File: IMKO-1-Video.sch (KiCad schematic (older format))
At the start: 20 parts, among them U18 82S129, U19 74LS244, U20 74LS244, U22 74LS32, U23 74LS86, U24 74LS163, U25 74LS00, U26 74LS374

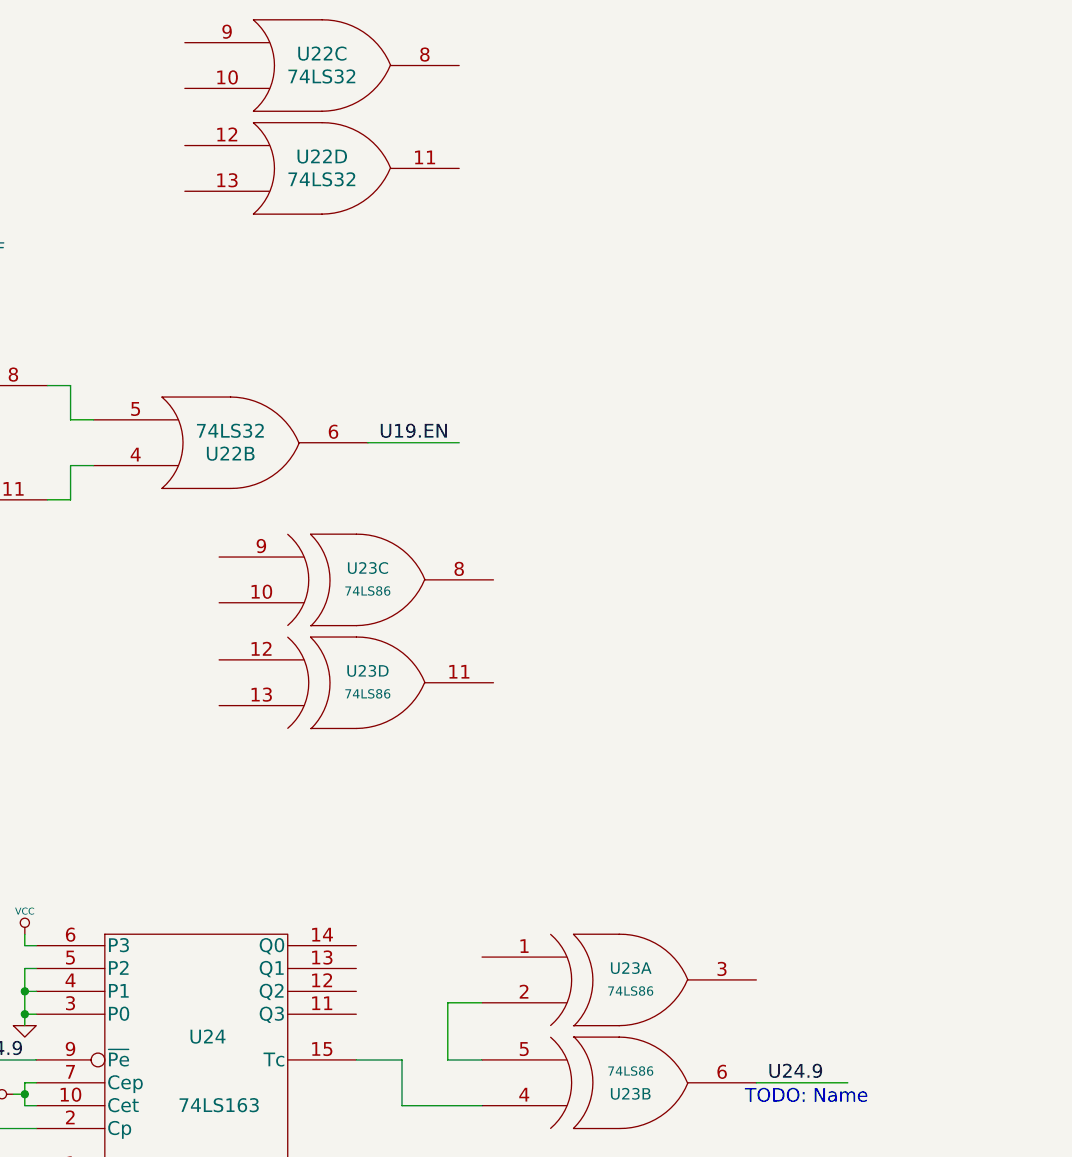
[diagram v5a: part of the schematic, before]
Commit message: Added SFF96364
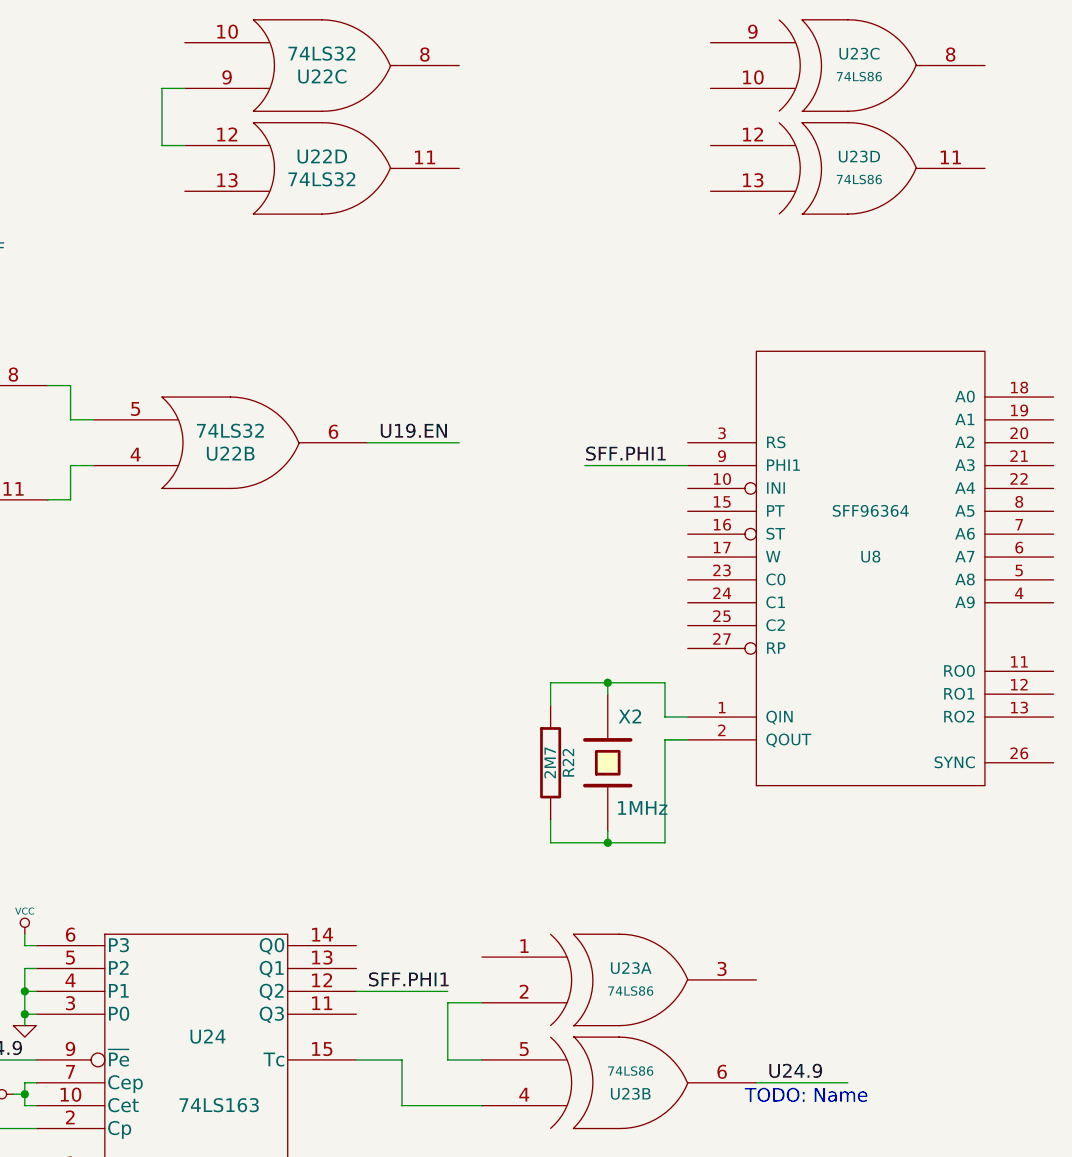
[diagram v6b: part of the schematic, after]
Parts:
- added R22: 2M7, symbol R
- added U8: SFF96364, MODULE, symbol SFF96364
- added X2: 1MHz, symbol CRYSTAL
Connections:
- net labels added: SFF.PHI1
- wire segments 148 -> 163
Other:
- moved on the sheet: U23C, U23D
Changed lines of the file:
@@
-EESchema Schematic File Version 2  date Wed 10 Oct 2012 11:46:42 PM EEST
+EESchema Schematic File Version 2  date Thu 11 Oct 2012 11:02:29 PM EEST
 LIBS:power
 LIBS:device
@@
 LIBS:valves
 LIBS:o_memory
+LIBS:SFF96364
 LIBS:IMKO-1-Video-cache
 EELAYER 27 0
@@
 Sheet 1 1
 Title "noname.sch"
-Date "10 oct 2012"
+Date "11 oct 2012"
 Rev ""
 Comp ""
@@
 L 74LS86 U23
 U 3 1 5075BC19
-P 9750 5300
-F 0 "U23" H 9800 5350 50  0000 C CNN
-F 1 "74LS86" H 9800 5250 40  0000 C CNN
-	3    9750 5300
+P 11900 3050
+F 0 "U23" H 11950 3100 50  0000 C CNN
+F 1 "74LS86" H 11950 3000 40  0000 C CNN
+	3    11900 3050
 	1    0    0    -1
 $EndComp
@@
 L 74LS86 U23
 U 4 1 5075BC2B
-P 9750 5750
-F 0 "U23" H 9800 5800 50  0000 C CNN
-F 1 "74LS86" H 9800 5700 40  0000 C CNN
-	4    9750 5750
+P 11900 3500
+F 0 "U23" H 11950 3550 50  0000 C CNN
+F 1 "74LS86" H 11950 3450 40  0000 C CNN
+	4    11900 3500
 	1    0    0    -1
 $EndComp
@@
 F 1 "74LS32" H 9600 3000 60  0000 C CNN
 	3    9600 3050
-	1    0    0    -1
+	1    0    0    1
 $EndComp
 $Comp
@@
 Text Label 4650 7600 0    60   ~ 0
 ~VID.INI
+$Comp
+L SFF96364 U8
+U 1 1 50771E3D
+P 12000 5100
+F 0 "U8" H 12000 5000 50  0000 C CNN
+F 1 "SFF96364" H 12000 5200 50  0000 C CNN
+F 2 "MODULE" H 12000 5100 50  0001 C CNN
+F 3 "DOCUMENTATION" H 12000 5100 50  0001 C CNN
+	1    12000 5100
+	1    0    0    -1
+$EndComp
+$Comp
+L CRYSTAL X2
+U 1 1 50771E58
+P 10850 6100
+F 0 "X2" V 11050 6000 60  0000 C CNN
+F 1 "1MHz" V 10650 5950 60  0000 C CNN
+	1    10850 6100
+	0    -1   -1   0
+$EndComp
+$Comp
+L R R22
+U 1 1 50771E7D
+P 10600 6100
+F 0 "R22" V 10680 6100 50  0000 C CNN
+F 1 "2M7" V 10600 6100 50  0000 C CNN
+	1    10600 6100
+	1    0    0    -1
+$EndComp
+Wire Wire Line
+	10600 6350 10600 6450
+Wire Wire Line
+	10600 5850 10600 5750
+Wire Wire Line
+	10600 5750 11100 5750
+Wire Wire Line
+	10850 5750 10850 5800
+Wire Wire Line
+	10600 6450 11100 6450
+Wire Wire Line
+	10850 6450 10850 6400
+Wire Wire Line
+	11100 5750 11100 5900
+Wire Wire Line
+	11100 5900 11200 5900
+Connection ~ 10850 5750
+Wire Wire Line
+	11100 6450 11100 6000
+Wire Wire Line
+	11100 6000 11200 6000
+Connection ~ 10850 6450
+Wire Wire Line
+	11200 4800 10750 4800
+Text Label 10750 4800 0    60   ~ 0
+SFF.PHI1
+Text Label 9800 7100 0    60   ~ 0
+SFF.PHI1
+Wire Wire Line
+	9750 7100 10150 7100
+Wire Wire Line
+	9000 3150 8900 3150
+Wire Wire Line
+	8900 3150 8900 3400
+Wire Wire Line
+	8900 3400 9000 3400
 $EndSCHEMATC

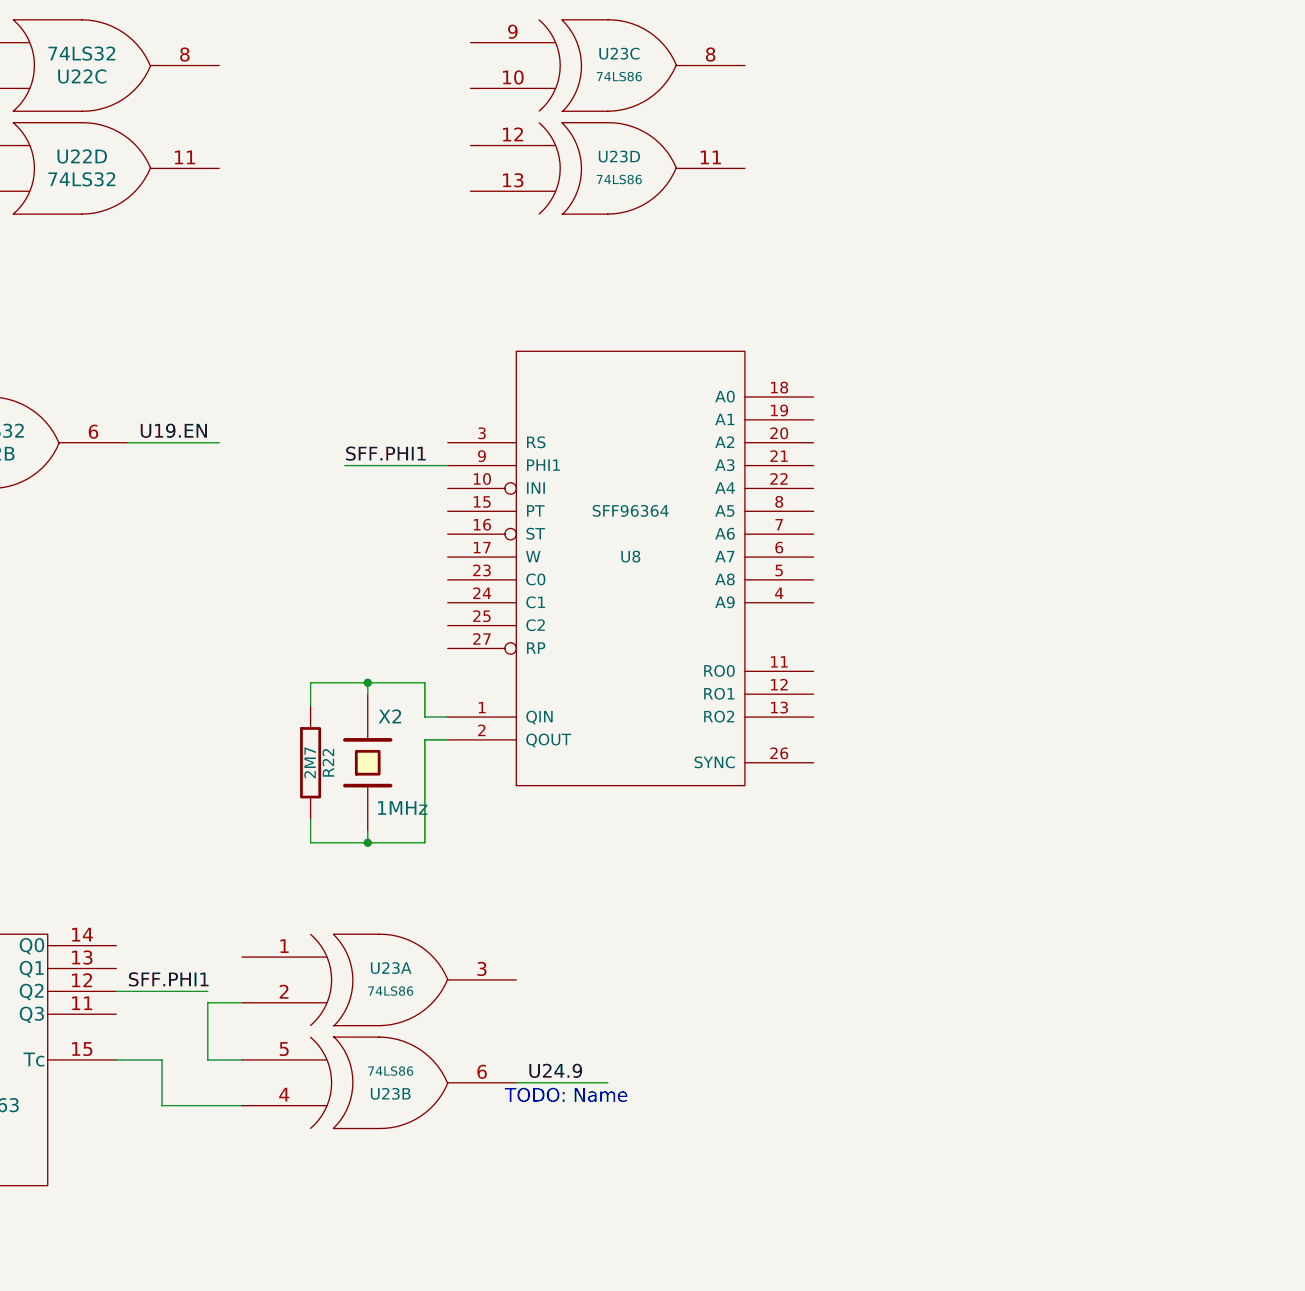
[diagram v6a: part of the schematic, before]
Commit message: Added Sync output
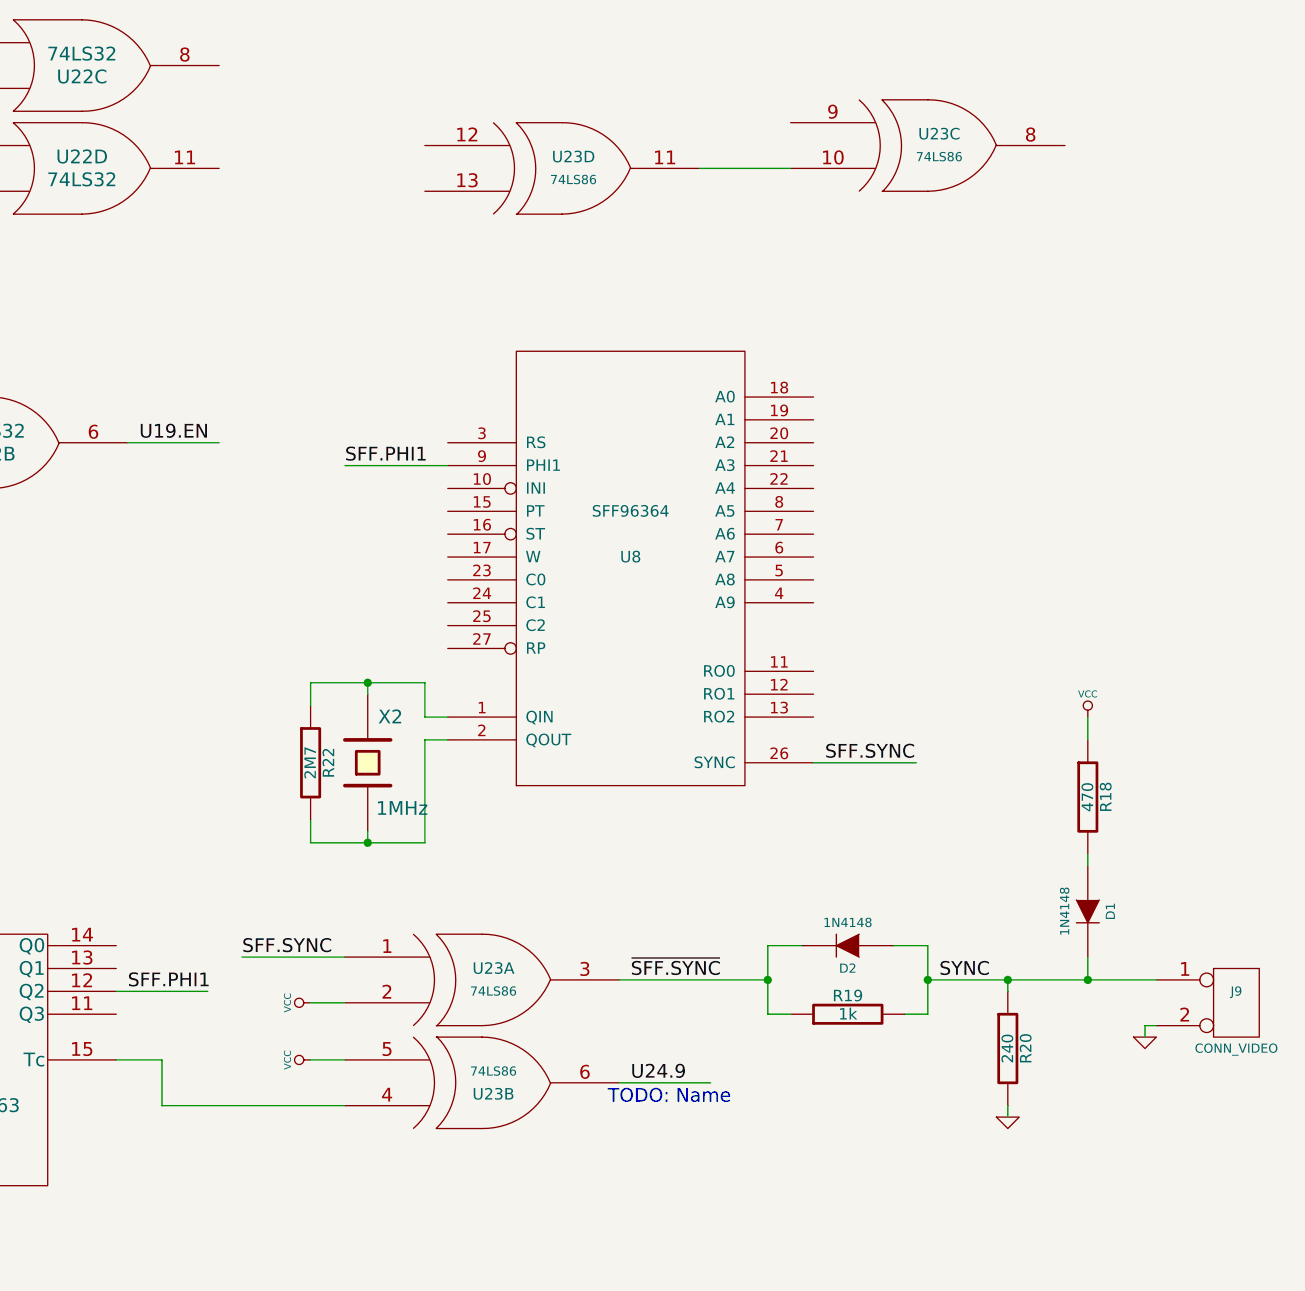
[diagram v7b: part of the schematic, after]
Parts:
- added D1, D2: 1N4148, symbol DIODE
- added J9: CONN_VIDEO, symbol CONN_2
- added R18: 470, symbol R
- added R19: 1k, symbol R
- added R20: 240, symbol R
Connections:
- net labels added: SFF.SYNC, SYNC, ~SFF.SYNC
- wire segments 163 -> 180
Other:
- moved on the sheet: U23A, U23B, U23C, U23D
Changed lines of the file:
@@
-EESchema Schematic File Version 2  date Thu 11 Oct 2012 11:02:29 PM EEST
+EESchema Schematic File Version 2  date Fri 12 Oct 2012 08:34:01 PM EEST
 LIBS:power
 LIBS:device
@@
 Sheet 1 1
 Title "noname.sch"
-Date "11 oct 2012"
+Date "12 oct 2012"
 Rev ""
 Comp ""
@@
 L 74LS86 U23
 U 1 1 5075BBEE
-P 10900 7050
-F 0 "U23" H 10950 7100 50  0000 C CNN
-F 1 "74LS86" H 10950 7000 40  0000 C CNN
-	1    10900 7050
+P 11350 7050
+F 0 "U23" H 11400 7100 50  0000 C CNN
+F 1 "74LS86" H 11400 7000 40  0000 C CNN
+	1    11350 7050
 	1    0    0    -1
 $EndComp
@@
 L 74LS86 U23
 U 2 1 5075BC07
-P 10900 7500
-F 0 "U23" H 10950 7550 50  0000 C CNN
-F 1 "74LS86" H 10950 7450 40  0000 C CNN
-	2    10900 7500
+P 11350 7500
+F 0 "U23" H 11400 7550 50  0000 C CNN
+F 1 "74LS86" H 11400 7450 40  0000 C CNN
+	2    11350 7500
 	1    0    0    1
 $EndComp
@@
 L 74LS86 U23
 U 3 1 5075BC19
-P 11900 3050
-F 0 "U23" H 11950 3100 50  0000 C CNN
-F 1 "74LS86" H 11950 3000 40  0000 C CNN
-	3    11900 3050
+P 13300 3400
+F 0 "U23" H 13350 3450 50  0000 C CNN
+F 1 "74LS86" H 13350 3350 40  0000 C CNN
+	3    13300 3400
 	1    0    0    -1
 $EndComp
@@
 L 74LS86 U23
 U 4 1 5075BC2B
-P 11900 3500
-F 0 "U23" H 11950 3550 50  0000 C CNN
-F 1 "74LS86" H 11950 3450 40  0000 C CNN
-	4    11900 3500
-	1    0    0    -1
-$EndComp
-Wire Wire Line
-	10300 7150 10150 7150
-Wire Wire Line
-	10300 7400 10150 7400
-Wire Wire Line
-	10150 7400 10150 7150
+P 11700 3500
+F 0 "U23" H 11750 3550 50  0000 C CNN
+F 1 "74LS86" H 11750 3450 40  0000 C CNN
+	4    11700 3500
+	1    0    0    -1
+$EndComp
+Wire Wire Line
+	10750 7150 10600 7150
+Wire Wire Line
+	10750 7400 10600 7400
 Wire Wire Line
 	9750 7400 9950 7400
@@
 	9950 7400 9950 7600
 Wire Wire Line
-	9950 7600 10300 7600
-Wire Wire Line
-	11500 7500 11900 7500
-Text Label 11550 7500 0    60   ~ 0
+	9950 7600 10750 7600
+Wire Wire Line
+	11950 7500 12350 7500
+Text Label 12000 7500 0    60   ~ 0
 U24.9
 Wire Wire Line
@@
 Text Label 8050 7400 0    60   ~ 0
 U24.9
-Text Notes 11450 7600 0    60   ~ 0
+Text Notes 11900 7600 0    60   ~ 0
 TODO: Name
 $Comp
@@
 Wire Wire Line
 	8900 3400 9000 3400
+Wire Wire Line
+	12800 6100 13250 6100
+Text Label 12850 6100 0    60   ~ 0
+SFF.SYNC
+Text Label 10300 6950 0    60   ~ 0
+SFF.SYNC
+Wire Wire Line
+	10300 6950 10750 6950
+Wire Wire Line
+	12300 3500 12700 3500
+$Comp
+L VCC #PWR023
+U 1 1 50784987
+P 10600 7150
+F 0 "#PWR023" H 10600 7250 30  0001 C CNN
+F 1 "VCC" H 10600 7250 30  0000 C CNN
+	1    10600 7150
+	0    -1   -1   0
+$EndComp
+$Comp
+L VCC #PWR024
+U 1 1 50784997
+P 10600 7400
+F 0 "#PWR024" H 10600 7500 30  0001 C CNN
+F 1 "VCC" H 10600 7500 30  0000 C CNN
+	1    10600 7400
+	0    -1   -1   0
+$EndComp
+Wire Wire Line
+	11950 7050 12600 7050
+Text Label 12000 7050 0    60   ~ 0
+~SFF.SYNC
+$Comp
+L DIODE D2
+U 1 1 50784D66
+P 12950 6900
+F 0 "D2" H 12950 7000 40  0000 C CNN
+F 1 "1N4148" H 12950 6800 40  0000 C CNN
+	1    12950 6900
+	-1   0    0    1
+$EndComp
+$Comp
+L R R19
+U 1 1 50784D75
+P 12950 7200
+F 0 "R19" V 13030 7200 50  0000 C CNN
+F 1 "1k" V 12950 7200 50  0000 C CNN
+	1    12950 7200
+	0    -1   -1   0
+$EndComp
+Wire Wire Line
+	12750 6900 12600 6900
+Wire Wire Line
+	12600 6900 12600 7200
+Wire Wire Line
+	12600 7200 12700 7200
+Connection ~ 12600 7050
+Wire Wire Line
+	13150 6900 13300 6900
+Wire Wire Line
+	13300 6900 13300 7200
+Wire Wire Line
+	13300 7200 13200 7200
+Wire Wire Line
+	13300 7050 14300 7050
+Connection ~ 13300 7050
+Text Label 13350 7050 0    60   ~ 0
+SYNC
+$Comp
+L R R20
+U 1 1 50785226
+P 13650 7350
+F 0 "R20" V 13730 7350 50  0000 C CNN
+F 1 "240" V 13650 7350 50  0000 C CNN
+	1    13650 7350
+	1    0    0    -1
+$EndComp
+$Comp
+L GND #PWR025
+U 1 1 5078523F
+P 13650 7650
+F 0 "#PWR025" H 13650 7650 30  0001 C CNN
+F 1 "GND" H 13650 7580 30  0001 C CNN
+	1    13650 7650
+	1    0    0    -1
+$EndComp
+Wire Wire Line
+	13650 7650 13650 7600
+Wire Wire Line
+	13650 7050 13650 7100
+$Comp
+L CONN_2 J9
+U 1 1 5078556A
+P 14650 7150
+F 0 "J9" H 14650 7200 40  0000 C CNN
+F 1 "CONN_VIDEO" H 14650 6950 40  0000 C CNN
+	1    14650 7150
+	1    0    0    -1
+$EndComp
+Connection ~ 13650 7050
+$Comp
+L DIODE D1
+U 1 1 5078565B
+P 14000 6750
+F 0 "D1" H 14000 6850 40  0000 C CNN
+F 1 "1N4148" H 14000 6650 40  0000 C CNN
+	1    14000 6750
+	0    1    1    0
+$EndComp
+Wire Wire Line
+	14000 6950 14000 7050
+Connection ~ 14000 7050
+$Comp
+L R R18
+U 1 1 507858D1
+P 14000 6250
+F 0 "R18" V 14080 6250 50  0000 C CNN
+F 1 "470" V 14000 6250 50  0000 C CNN
+	1    14000 6250
+	1    0    0    -1
+$EndComp
+$Comp
+L VCC #PWR026
+U 1 1 507858D7
+P 14000 5900
+F 0 "#PWR026" H 14000 6000 30  0001 C CNN
+F 1 "VCC" H 14000 6000 30  0000 C CNN
+	1    14000 5900
+	1    0    0    -1
+$EndComp
+Wire Wire Line
+	14000 5900 14000 6000
+Wire Wire Line
+	14000 6500 14000 6550
+$Comp
+L GND #PWR027
+U 1 1 50785C17
+P 14250 7300
+F 0 "#PWR027" H 14250 7300 30  0001 C CNN
+F 1 "GND" H 14250 7230 30  0001 C CNN
+	1    14250 7300
+	1    0    0    -1
+$EndComp
+Wire Wire Line
+	14300 7250 14250 7250
+Wire Wire Line
+	14250 7250 14250 7300
 $EndSCHEMATC
